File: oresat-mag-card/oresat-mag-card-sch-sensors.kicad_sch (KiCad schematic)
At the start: 22 parts, among them U10 LTC4300A-1, U11 MAX892LEUA+T, U9 ICM-42688-P

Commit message: Small update
removed all traces containing widths of .127 and widened to .2, and some other small misc items
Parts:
- R49, R50, R51, R53, R54, R55, R56: footprint Resistor_SMD:R_0603_1608Metric -> oresat-passives:c_0603-SMALL
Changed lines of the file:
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@@
 			)
 		)
-		(property "Footprint" "Resistor_SMD:R_0603_1608Metric"
+		(property "Footprint" "oresat-passives:c_0603-SMALL"
 			(at 304.8 156.21 0)
 			(effects
@@
 			)
 		)
-		(property "Footprint" "Resistor_SMD:R_0603_1608Metric"
+		(property "Footprint" "oresat-passives:c_0603-SMALL"
 			(at 278.13 251.46 0)
 			(effects
@@
 			)
 		)
-		(property "Footprint" "Resistor_SMD:R_0603_1608Metric"
+		(property "Footprint" "oresat-passives:c_0603-SMALL"
 			(at 208.28 54.61 0)
 			(effects
@@
 			)
 		)
-		(property "Footprint" "Resistor_SMD:R_0603_1608Metric"
+		(property "Footprint" "oresat-passives:c_0603-SMALL"
 			(at 231.14 219.71 0)
 			(effects
@@
 			)
 		)
-		(property "Footprint" "Resistor_SMD:R_0603_1608Metric"
+		(property "Footprint" "oresat-passives:c_0603-SMALL"
 			(at 295.91 156.21 0)
 			(effects
@@
 			)
 		)
-		(property "Footprint" "Resistor_SMD:R_0603_1608Metric"
+		(property "Footprint" "oresat-passives:c_0603-SMALL"
 			(at 238.76 219.71 0)
 			(effects
@@
 			)
 		)
-		(property "Footprint" "Resistor_SMD:R_0603_1608Metric"
+		(property "Footprint" "oresat-passives:c_0603-SMALL"
 			(at 284.48 148.59 0)
 			(effects

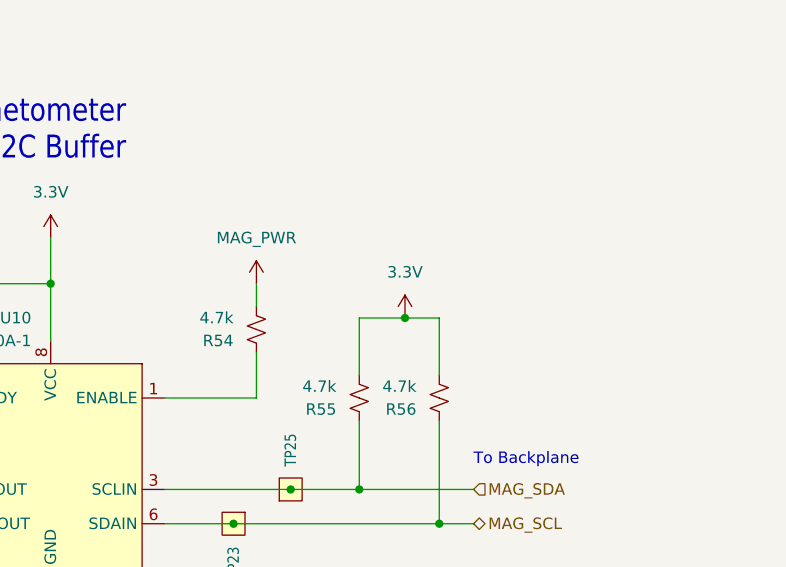
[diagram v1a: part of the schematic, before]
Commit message: Update
Updated footprints, symbols, and pcb layout to have IMU in center of board.
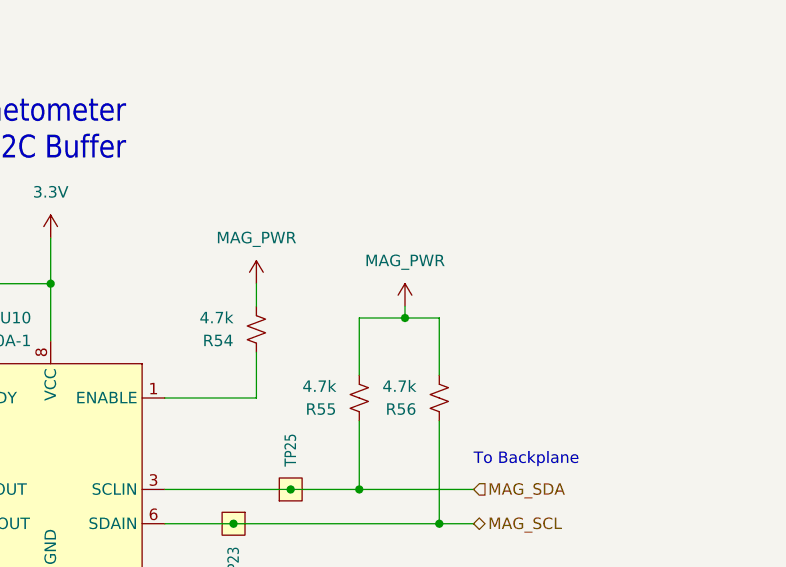
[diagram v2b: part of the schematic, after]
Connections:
- net 3.3V: no longer R55.2, R56.2
- net MAG_PWR: now also R55.2, R56.2
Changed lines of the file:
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@@
+	)
+	(junction
+		(at 300.99 147.32)
+		(diameter 0)
+		(color 0 0 0 0)
 	)
 	(junction
@@
 	)
 	(junction
-		(at 300.99 147.32)
-		(diameter 0)
-		(color 0 0 0 0)
-	)
-	(junction
 		(at 238.76 240.03)
 		(diameter 0)
@@
 	(wire
 		(pts
+			(xy 300.99 147.32) (xy 304.8 147.32)
+		)
+		(stroke
+			(width 0)
+			(type default)
+		)
+	)
+	(wire
+		(pts
 			(xy 261.62 143.51) (xy 261.62 138.43)
 		)
@@
 	(wire
 		(pts
+			(xy 295.91 147.32) (xy 300.99 147.32)
+		)
+		(stroke
+			(width 0)
+			(type default)
+		)
+	)
+	(wire
+		(pts
 			(xy 304.8 147.32) (xy 304.8 153.67)
 		)
@@
 	(wire
 		(pts
-			(xy 295.91 147.32) (xy 300.99 147.32)
-		)
-		(stroke
-			(width 0)
-			(type default)
-		)
-	)
-	(wire
-		(pts
 			(xy 304.8 158.75) (xy 304.8 170.18)
 		)
@@
 	(wire
 		(pts
+			(xy 300.99 146.05) (xy 300.99 147.32)
+		)
+		(stroke
+			(width 0)
+			(type default)
+		)
+	)
+	(wire
+		(pts
 			(xy 290.83 73.66) (xy 287.02 73.66)
 		)
@@
 		(pts
 			(xy 246.38 213.36) (xy 238.76 213.36)
-		)
-		(stroke
-			(width 0)
-			(type default)
-		)
-	)
-	(wire
-		(pts
-			(xy 300.99 147.32) (xy 304.8 147.32)
 		)
 		(stroke
@@
 			)
 			(justify right)
-		)
-	)
-	(symbol
-		(lib_id "oresat-power:3.3V")
-		(at 300.99 147.32 0)
-		(unit 1)
-		(exclude_from_sim no)
-		(in_bom yes)
-		(on_board yes)
-		(dnp no)
-		(fields_autoplaced yes)
-		(property "Reference" "#3V014"
-			(at 300.99 151.13 0)
-			(effects
-				(font
-					(size 1.27 1.27)
-				)
-				(hide yes)
-			)
-		)
-		(property "Value" "3.3V"
-			(at 300.99 142.24 0)
-			(effects
-				(font
-					(size 1.27 1.27)
-				)
-			)
-		)
-		(property "Footprint" ""
-			(at 300.99 147.32 0)
-			(effects
-				(font
-					(size 1.27 1.27)
-				)
-				(hide yes)
-			)
-		)
-		(property "Datasheet" ""
-			(at 300.99 147.32 0)
-			(effects
-				(font
-					(size 1.27 1.27)
-				)
-				(hide yes)
-			)
-		)
-		(property "Description" "Power symbol creates a global label with name \"3.3V\""
-			(at 300.99 147.32 0)
-			(effects
-				(font
-					(size 1.27 1.27)
-				)
-				(hide yes)
-			)
-		)
-		(pin "1"
-		)
-		(instances
-			(project "oresat-mag-card"
-				(path "/c58960d9-4cac-4036-ad2e-1aef26946dae/a4e22a47-8081-427b-a284-fdb057c6b905"
-					(reference "#3V014")
-					(unit 1)
-				)
-			)
 		)
 	)
@@
 					(unit 1)
 				)
+			)
+		)
+	)
+	(symbol
+		(lib_id "power:VCC")
+		(at 300.99 146.05 0)
+		(unit 1)
+		(exclude_from_sim no)
+		(in_bom yes)
+		(on_board yes)
+		(dnp no)
+		(fields_autoplaced yes)
+		(property "Reference" "#MAG_PWR04"
+			(at 300.99 149.86 0)
+			(effects
+				(font
+					(size 1.27 1.27)
+				)
+				(hide yes)
+			)
+		)
+		(property "Value" "MAG_PWR"
+			(at 300.99 140.97 0)
+			(effects
+				(font
+					(size 1.27 1.27)
+				)
+			)
+		)
+		(property "Footprint" ""
+			(at 300.99 146.05 0)
+			(effects
+				(font
+					(size 1.27 1.27)
+				)
+				(hide yes)
+			)
+		)
+		(property "Datasheet" ""
+			(at 300.99 146.05 0)
+			(effects
+				(font
+					(size 1.27 1.27)
+				)
+				(hide yes)
+			)
+		)
+		(property "Description" "Power symbol creates a global label with name \"VCC\""
+			(at 300.99 146.05 0)
+			(effects
+				(font
+					(size 1.27 1.27)
+				)
+				(hide yes)
+			)
+		)
+		(pin "1"
+		)
+		(instances
+			(project "oresat-mag-card"
+				(path "/c58960d9-4cac-4036-ad2e-1aef26946dae/a4e22a47-8081-427b-a284-fdb057c6b905"
+					(reference "#MAG_PWR04")
+					(unit 1)
+				)

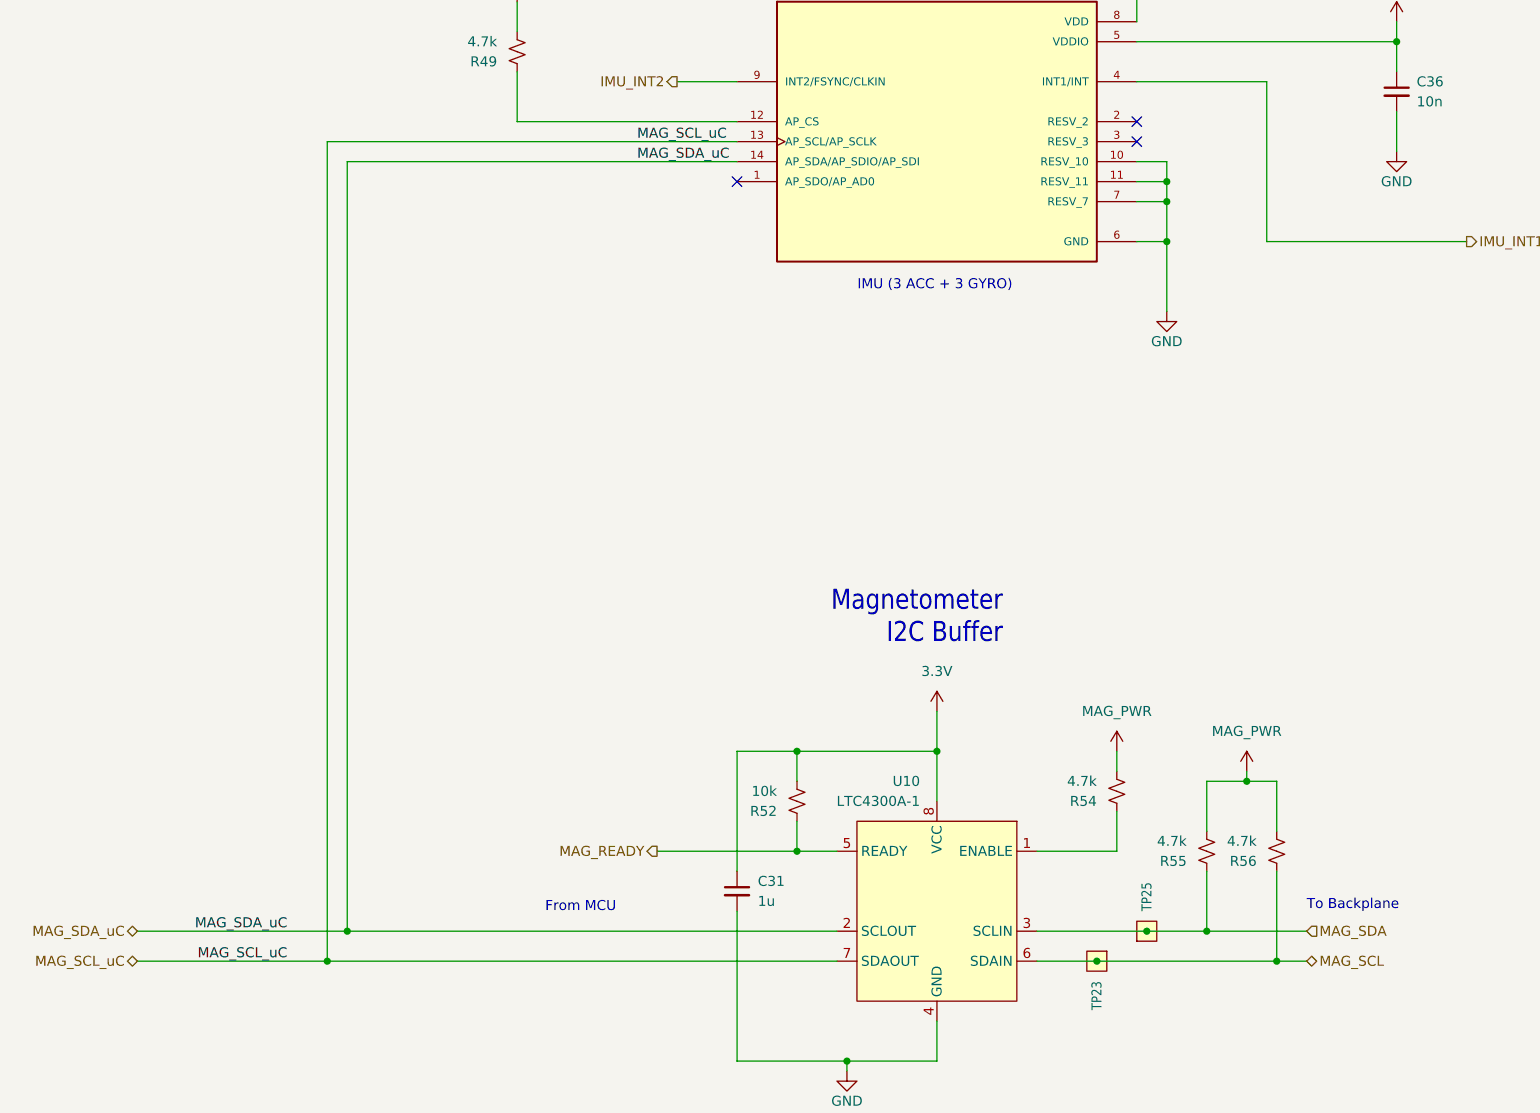
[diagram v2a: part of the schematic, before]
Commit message: Final Push
Updated I2C buffer because SCL and SDA were swapped, added copper backfill to layer 3. Added extra caps to u3 and u2.
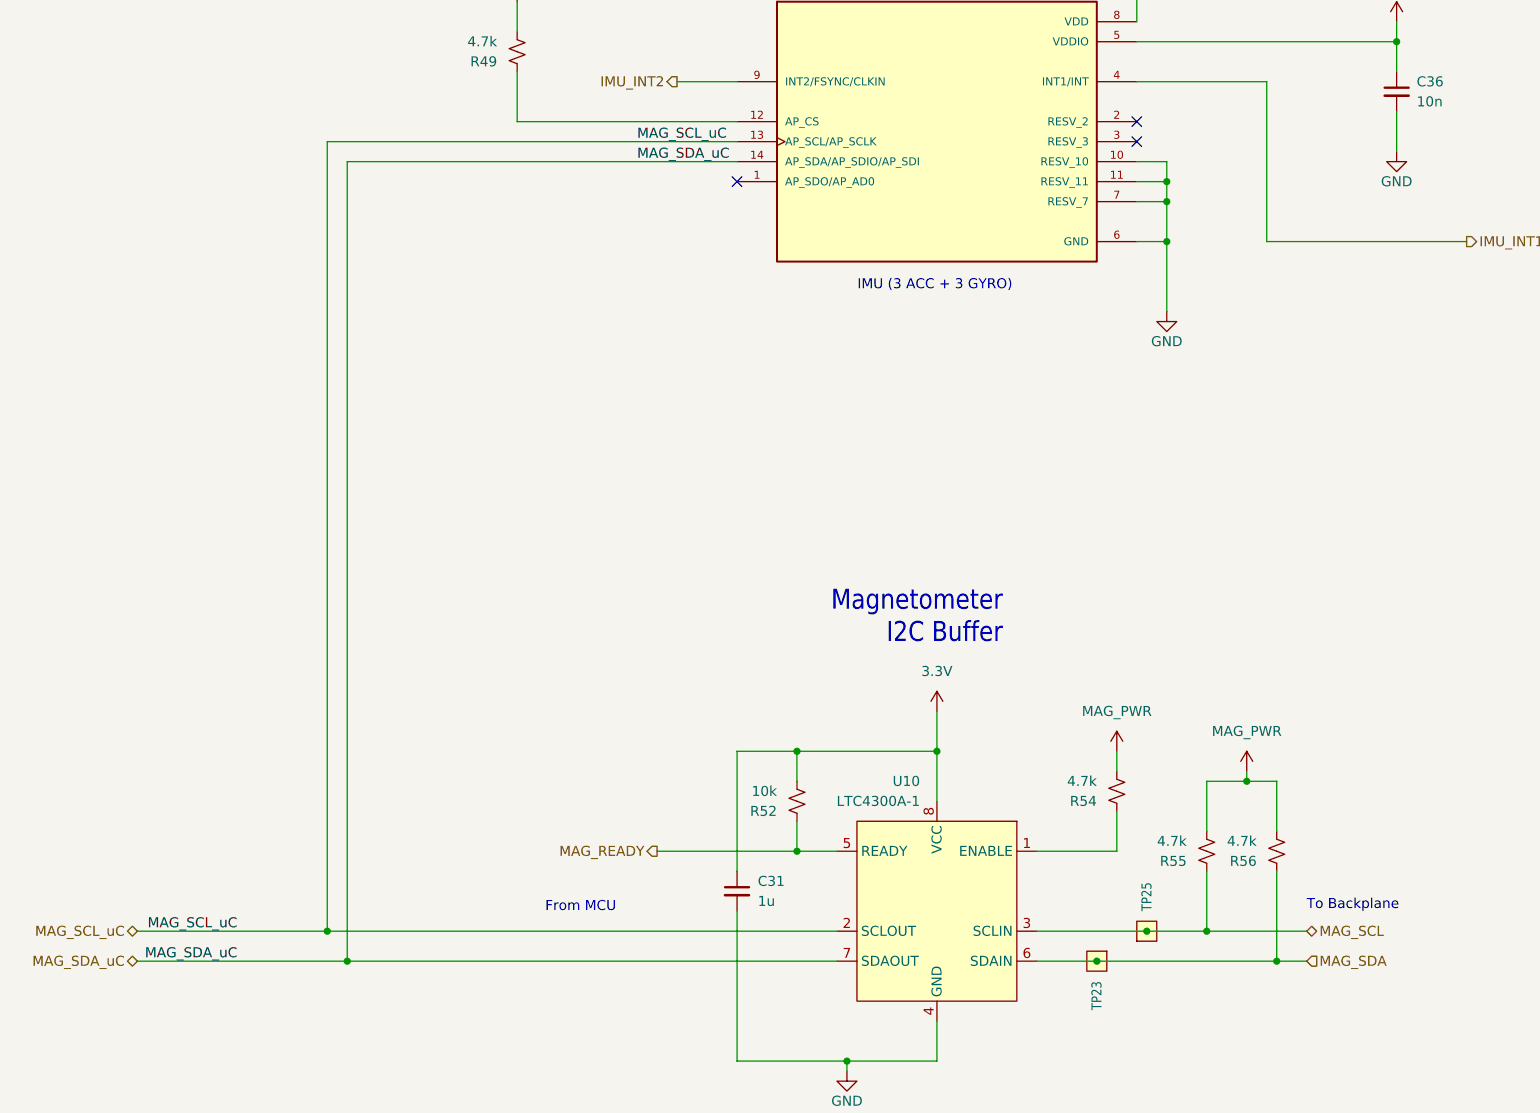
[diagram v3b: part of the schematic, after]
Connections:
- net MAG_SCL: now also R55.1, TP25.1, U10.3 (SCLIN); no longer R56.1, TP23.1, U10.6 (SDAIN)
- net MAG_SCL_uC: now also U10.2 (SCLOUT); no longer U10.7 (SDAOUT)
- net MAG_SDA: now also R56.1, TP23.1, U10.6 (SDAIN); no longer R55.1, TP25.1, U10.3 (SCLIN)
- net MAG_SDA_uC: now also U10.7 (SDAOUT); no longer U10.2 (SCLOUT)
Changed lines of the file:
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@@
+	)
+	(junction
+		(at 186.69 170.18)
+		(diameter 0)
+		(color 0 0 0 0)
 	)
 	(junction
@@
 	)
 	(junction
-		(at 186.69 166.37)
+		(at 184.15 166.37)
 		(diameter 0)
 		(color 0 0 0 0)
@@
 	(junction
 		(at 290.83 73.66)
-		(diameter 0)
-		(color 0 0 0 0)
-	)
-	(junction
-		(at 184.15 170.18)
 		(diameter 0)
 		(color 0 0 0 0)
@@
 	(wire
 		(pts
+			(xy 186.69 68.58) (xy 186.69 170.18)
+		)
+		(stroke
+			(width 0)
+			(type default)
+		)
+	)
+	(wire
+		(pts
 			(xy 287.02 24.13) (xy 294.64 24.13)
 		)
@@
 	(wire
 		(pts
-			(xy 160.02 166.37) (xy 186.69 166.37)
+			(xy 160.02 166.37) (xy 184.15 166.37)
 		)
 		(stroke
@@
 	(wire
 		(pts
-			(xy 186.69 166.37) (xy 248.92 166.37)
+			(xy 184.15 166.37) (xy 248.92 166.37)
 		)
 		(stroke
@@
 	(wire
 		(pts
-			(xy 184.15 170.18) (xy 184.15 66.04)
-		)
-		(stroke
-			(width 0)
-			(type default)
-		)
-	)
-	(wire
-		(pts
 			(xy 300.99 31.75) (xy 300.99 38.1)
 		)
@@
 	(wire
 		(pts
+			(xy 186.69 170.18) (xy 248.92 170.18)
+		)
+		(stroke
+			(width 0)
+			(type default)
+		)
+	)
+	(wire
+		(pts
 			(xy 248.92 156.21) (xy 243.84 156.21)
 		)
@@
 	(wire
 		(pts
+			(xy 184.15 66.04) (xy 184.15 166.37)
+		)
+		(stroke
+			(width 0)
+			(type default)
+		)
+	)
+	(wire
+		(pts
 			(xy 295.91 147.32) (xy 295.91 153.67)
 		)
@@
 	(wire
 		(pts
-			(xy 160.02 170.18) (xy 184.15 170.18)
-		)
-		(stroke
-			(width 0)
-			(type default)
-		)
-	)
-	(wire
-		(pts
 			(xy 243.84 143.51) (xy 243.84 147.32)
 		)
@@
 	(wire
 		(pts
-			(xy 186.69 166.37) (xy 186.69 68.58)
-		)
-		(stroke
-			(width 0)
-			(type default)
-		)
-	)
-	(wire
-		(pts
 			(xy 284.48 156.21) (xy 274.32 156.21)
 		)
@@
 	(wire
 		(pts
-			(xy 184.15 170.18) (xy 248.92 170.18)
+			(xy 160.02 170.18) (xy 186.69 170.18)
 		)
 		(stroke
@@
 	)
 	(label "MAG_SCL_uC"
-		(at 179.07 170.18 180)
+		(at 172.72 166.37 180)
 		(effects
 			(font
@@
 	)
 	(label "MAG_SDA_uC"
-		(at 179.07 166.37 180)
+		(at 172.72 170.18 180)
 		(effects
 			(font
@@
 			)
 			(justify left bottom)
+		)
+	)
+	(hierarchical_label "MAG_SCL_uC"
+		(shape bidirectional)
+		(at 160.02 166.37 180)
+		(effects
+			(font
+				(size 1.27 1.27)
+			)
+			(justify right)
 		)
 	)
@@
 		)
 	)
+	(hierarchical_label "MAG_SCL"
+		(shape bidirectional)
+		(at 308.61 166.37 0)
+		(effects
+			(font
+				(size 1.27 1.27)
+			)
+			(justify left)
+		)
+	)
 	(hierarchical_label "MAG_SDA_uC"
 		(shape bidirectional)
-		(at 160.02 166.37 180)
+		(at 160.02 170.18 180)
 		(effects
 			(font
@@
 		)
 	)
+	(hierarchical_label "MAG_SDA"
+		(shape input)
+		(at 308.61 170.18 0)
+		(effects
+			(font
+				(size 1.27 1.27)
+			)
+			(justify left)
+		)
+	)
 	(hierarchical_label "MAG_~{FAULT}"
 		(shape input)
@@
 		)
 	)
-	(hierarchical_label "MAG_SDA"
-		(shape input)
-		(at 308.61 166.37 0)
-		(effects
-			(font
-				(size 1.27 1.27)
-			)
-			(justify left)
-		)
-	)
-	(hierarchical_label "MAG_SCL"
-		(shape bidirectional)
-		(at 308.61 170.18 0)
-		(effects
-			(font
-				(size 1.27 1.27)
-			)
-			(justify left)
-		)
-	)
-	(hierarchical_label "MAG_SCL_uC"
-		(shape bidirectional)
-		(at 160.02 170.18 180)
-		(effects
-			(font
-				(size 1.27 1.27)
-			)
-			(justify right)
-		)
-	)
